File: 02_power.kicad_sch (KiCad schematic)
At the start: 24 parts, among them J4 USB4105-GF-A, J6 Conn_01x02_Socket, Q2 DMG2305UX-7, U2 BQ24090DGQ

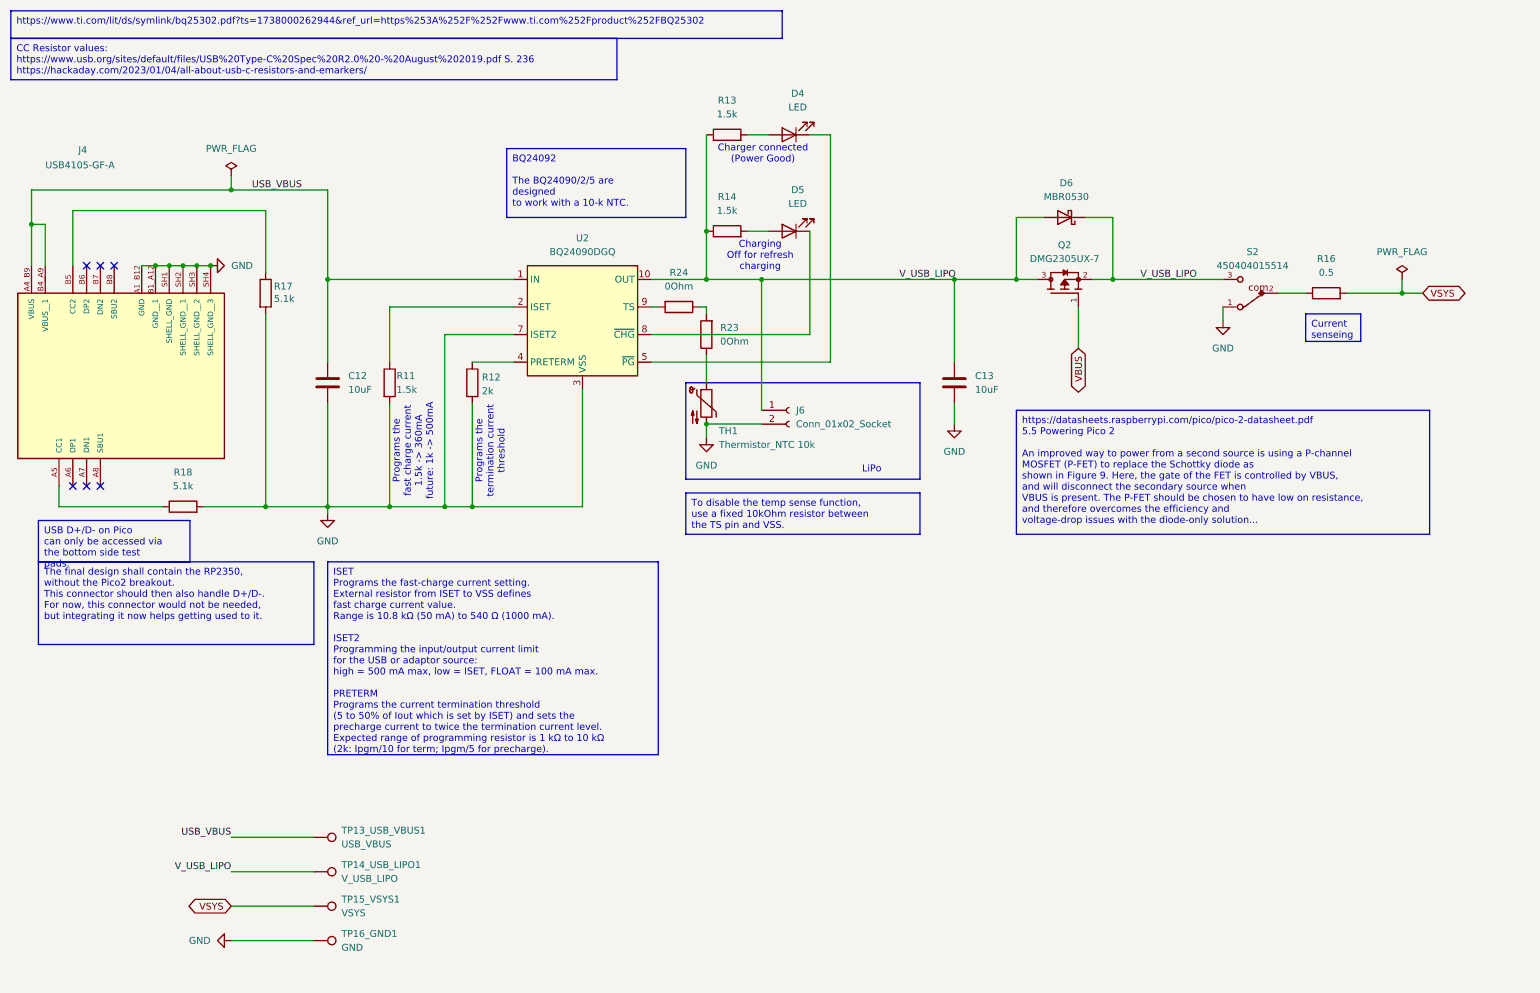
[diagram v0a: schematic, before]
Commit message: Migrate to KiCad 9, start working on the new revision
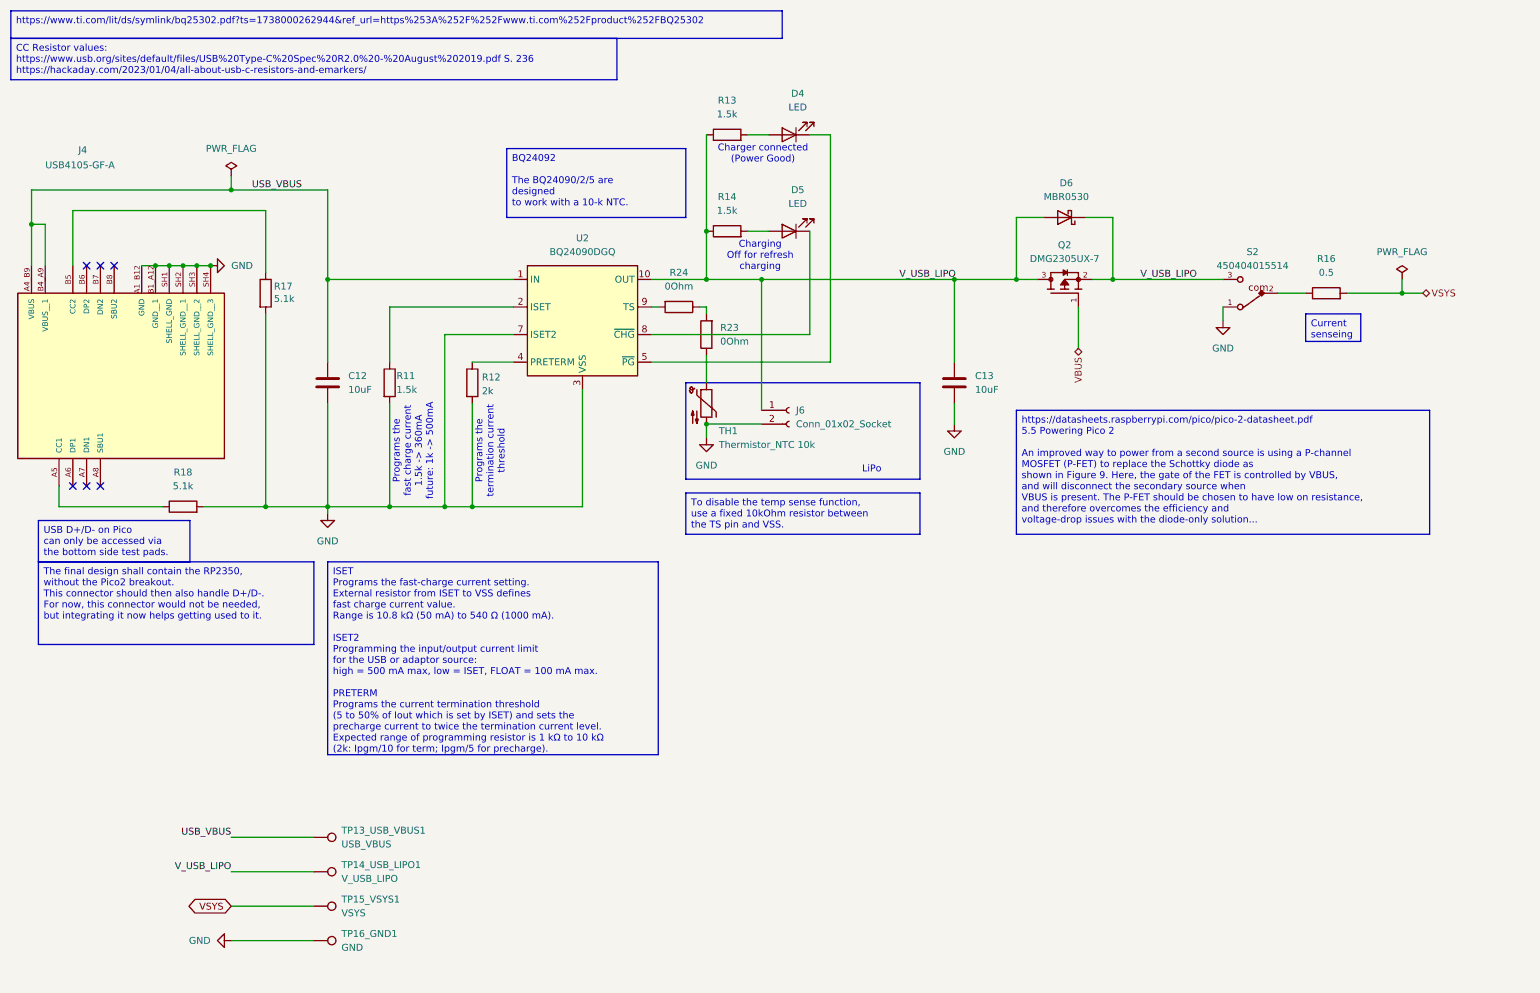
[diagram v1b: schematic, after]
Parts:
- Q2: Description_1 MOSFET P-Ch 20V 5A Enhancement SOT23 | Diodes Inc DMG2305UX-7 -> MOSFET P-Ch 20V 5A Enhancement SOT23 | Diodes Inc DMG2305UX-7
- S2: Description_1 Slide Switch SPDT Surface Mount -> Slide Switch SPDT Surface Mount

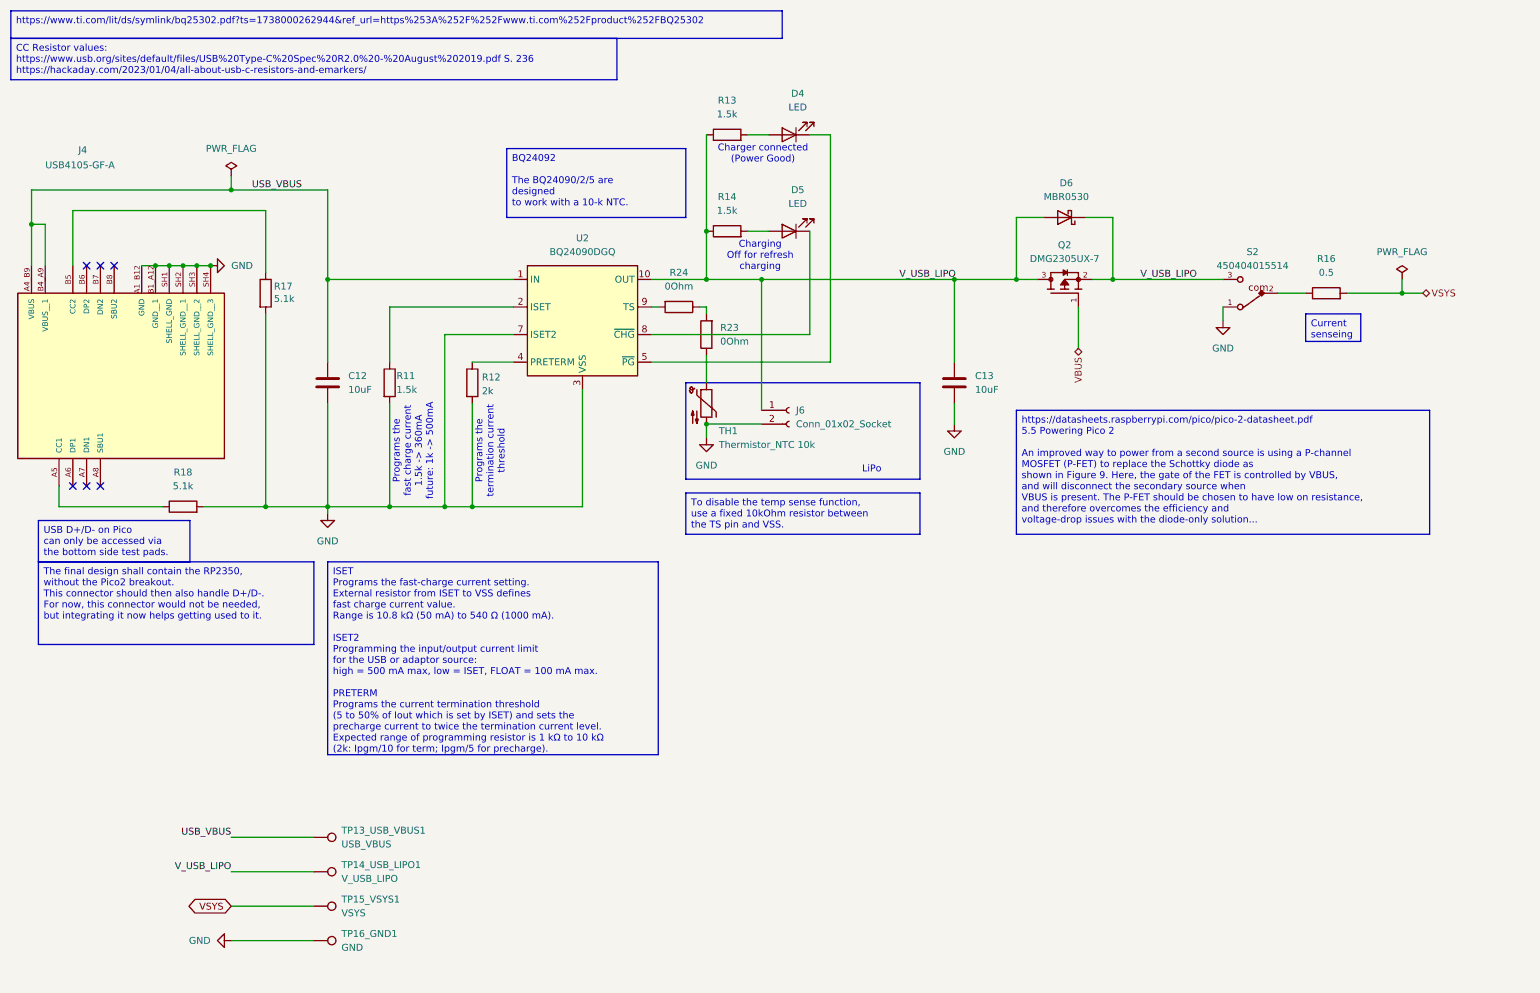
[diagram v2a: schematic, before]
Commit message: updated power path, connect USB-C to pico's USB data
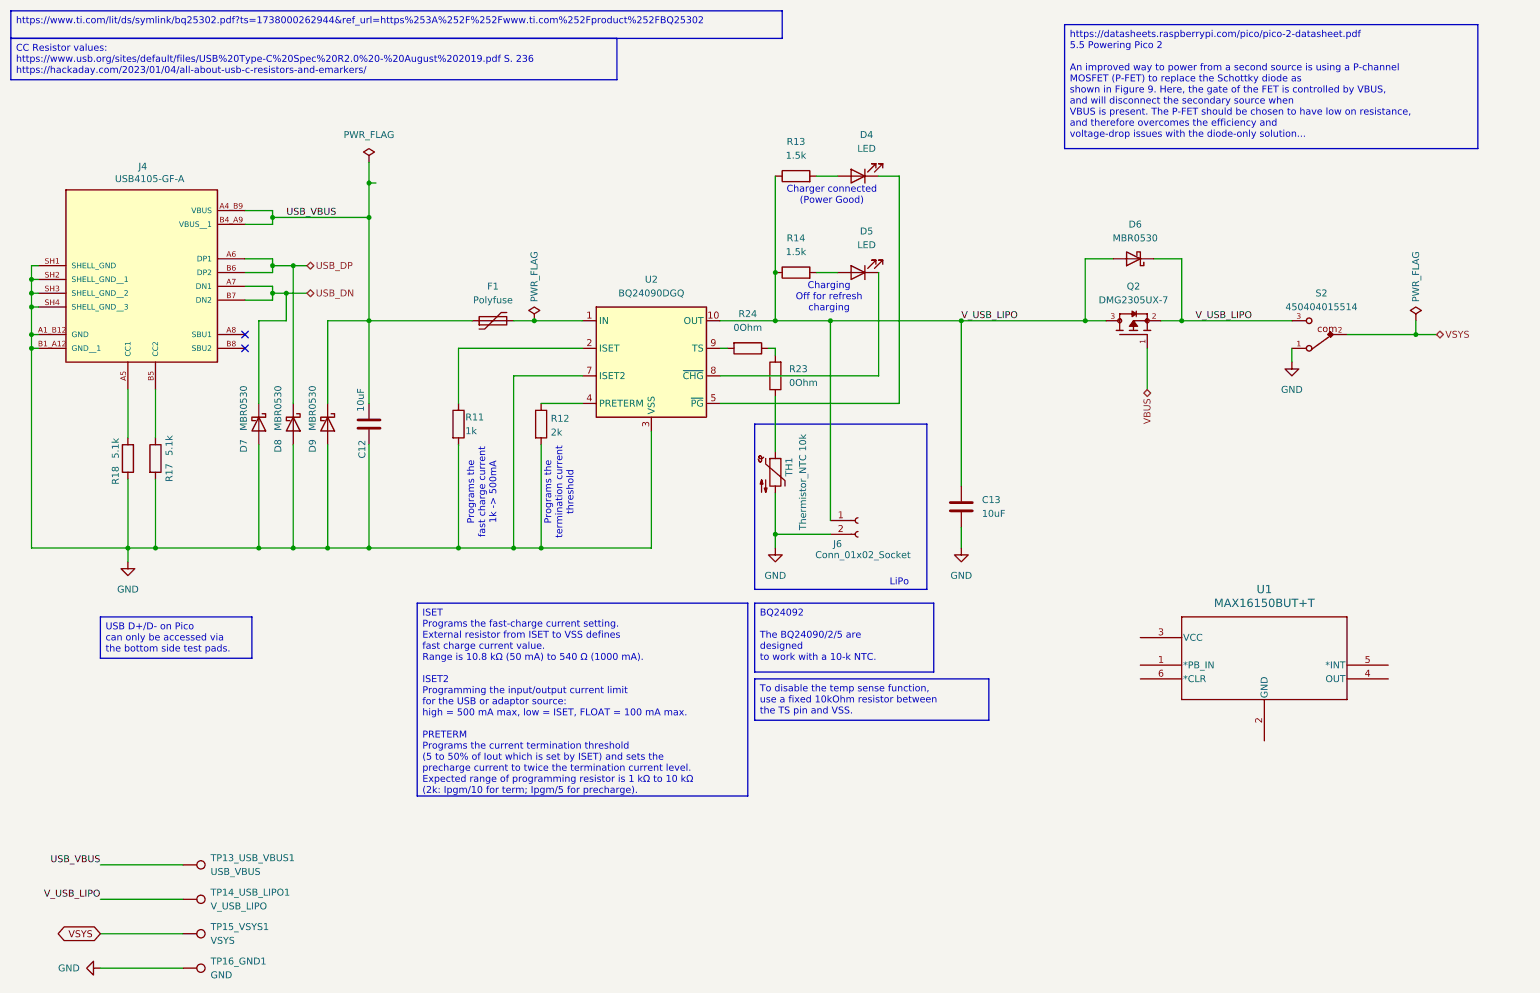
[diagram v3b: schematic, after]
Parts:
- removed R16: 0.5, Resistor_SMD:R_1206_3216Metric_Pad1.30x1.75mm_HandSolder, symbol Device:R
- added D7, D8, D9: MBR0530, Diode_SMD:D_SOD-123, symbol Diode:MBR0530
- added F1: Polyfuse, symbol Device:Polyfuse
- added U1: MAX16150BUT+T, prj-footprints:21-0058I_MXM-M, symbol MAX16150BUT+T:MAX16150BUT+T
- J4: symbol USB4105-GF-A:USB4105-GF-A -> my-usb4105-gf-a:USB4105-GF-A
- R11: value 1.5k -> 1k
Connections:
- net GND: now also R18.1, D7.2 (A), D8.2 (A), D9.2 (A); no longer R18.2
- net USB_VBUS: now also D9.1 (K), F1.1; no longer U2.1 (IN)
- net VSYS: now also S2.2
- net at J4.A5 (CC1): now also R18.2; no longer R18.1
- net USB_DP: now reaches J4.A6 (DP1)
- net USB_DP: now also J4.B6 (DP2), D8.1 (K)
- net USB_DN: now reaches J4.A7 (DN1)
- net USB_DN: now also J4.B7 (DN2), D7.1 (K)
- new net: F1.2, U2.1 (IN)
- no-connect marks 6 -> 2
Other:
- note added: "Programs the fast charge current 1k -> 500mA"
- note removed: "Programs the fast charge current 1.5k -> 360mA future: 1k -> 500mA"
- moved on the sheet: C12, C13, D4, D5, D6, J4, J6, Q2, R11, R12, R13, R14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
